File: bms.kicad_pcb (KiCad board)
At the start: 4 copper layers, 100 x 67 mm, 179 parts, among them J1 CELL_TAPS, J2 I2C_IN, J3 THERM_1, J4 THERM_2, J5 SWD, Q1 AO3400A, Q10 AO3400A, Q11 AO3400A, Q12 AO3400A, Q13 AO3400A, Q14 AO3400A, Q15 AO3400A, Q16 AO3400A, Q17 AO3400A, Q18 AO3400A, Q19 AO3400A, Q2 AO3400A, Q20 AO3400A, Q3 AO3400A, Q4 AO3400A, Q5 AO3400A, Q6 AO3400A, Q7 AO3400A, Q8 AO3400A, Q9 AO3400A, SW1 SW_Push, U1 LMR516xx, U2 STM32F103C8Tx, U3 ADuM1252, U4 MAX14920, U5 MAX11163, U6 MAX6126, Y1 8M

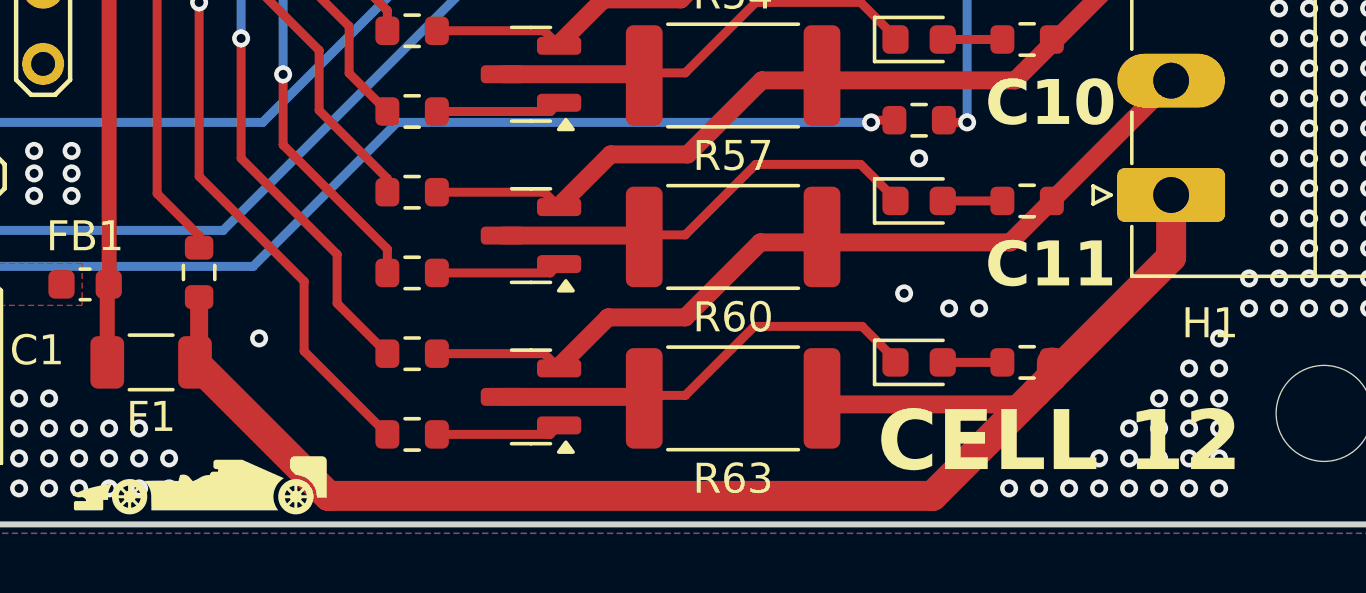
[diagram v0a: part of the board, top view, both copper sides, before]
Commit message: pcb: Reduce TAP12 trace width from 1 mm to 0.6 mm
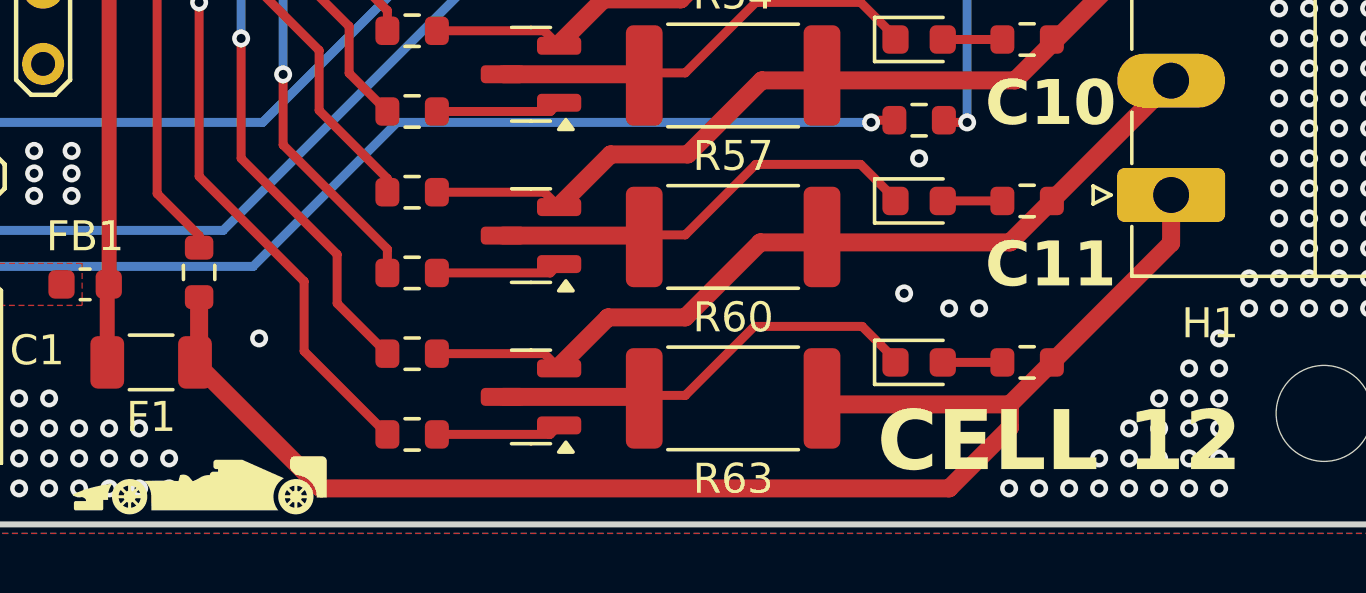
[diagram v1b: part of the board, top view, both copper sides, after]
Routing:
- net TAP12: track 49.8 -> 48.3 mm
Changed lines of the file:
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@@
 	(segment
 		(start 136.4 110.22)
-		(end 136.4 112.3)
-		(width 1)
+		(end 136.4 111.825)
+		(width 0.6)
 		(layer "F.Cu")
 		(net 70)
 	)
 	(segment
-		(start 128.45 120.25)
-		(end 131.9 116.8)
-		(width 1)
+		(start 131.025 117.2)
+		(end 132.425 115.8)
+		(width 0.6)
 		(layer "F.Cu")
 		(net 70)
@@
 	)
 	(segment
-		(start 136.4 112.3)
-		(end 132.425 116.275)
-		(width 1)
-		(layer "F.Cu")
-		(net 70)
-	)
-	(segment
-		(start 103.8625 115.8)
-		(end 108.3125 120.25)
-		(width 1)
-		(layer "F.Cu")
-		(net 70)
-	)
-	(segment
 		(start 104 115.6625)
 		(end 103.8625 115.8)
@@
 	)
 	(segment
-		(start 132.425 115.8)
-		(end 132.425 116.275)
-		(width 1)
+		(start 129 120)
+		(end 108.0625 120)
+		(width 0.6)
+		(layer "F.Cu")
+		(net 70)
+	)
+	(segment
+		(start 136.4 111.825)
+		(end 132.425 115.8)
+		(width 0.6)
+		(layer "F.Cu")
+		(net 70)
+	)
+	(segment
+		(start 131.025 117.975)
+		(end 131.025 117.2)
+		(width 0.6)
+		(layer "F.Cu")
+		(net 70)
+	)
+	(segment
+		(start 108.0625 120)
+		(end 103.8625 115.8)
+		(width 0.6)
 		(layer "F.Cu")
 		(net 70)
@@
 	(segment
 		(start 124.9625 117.2)
-		(end 131.5 117.2)
+		(end 131.025 117.2)
 		(width 0.6)
 		(layer "F.Cu")
@@
 	)
 	(segment
-		(start 108.3125 120.25)
-		(end 128.45 120.25)
-		(width 1)
-		(layer "F.Cu")
-		(net 70)
-	)
-	(segment
-		(start 132.425 116.275)
-		(end 131.9 116.8)
-		(width 1)
+		(start 129 120)
+		(end 131.025 117.975)
+		(width 0.6)
 		(layer "F.Cu")
 		(net 70)
@@
 		(width 0.6)
 		(layer "F.Cu")
-		(net 70)
-	)
-	(segment
-		(start 131.5 117.2)
-		(end 131.9 116.8)
-		(width 0.6)
-		(layer "F.Cu")

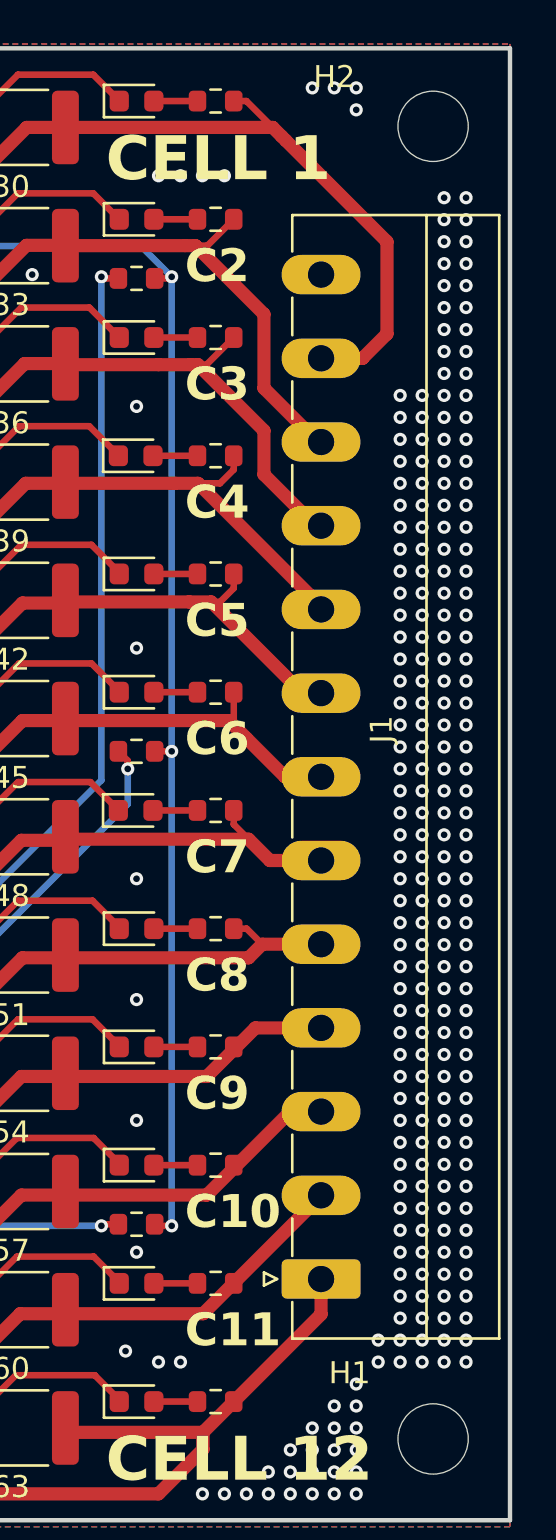
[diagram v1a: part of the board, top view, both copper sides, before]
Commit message: pcb: Move cell tap connector towards board edge by 0.3 mm
Closes GH-1
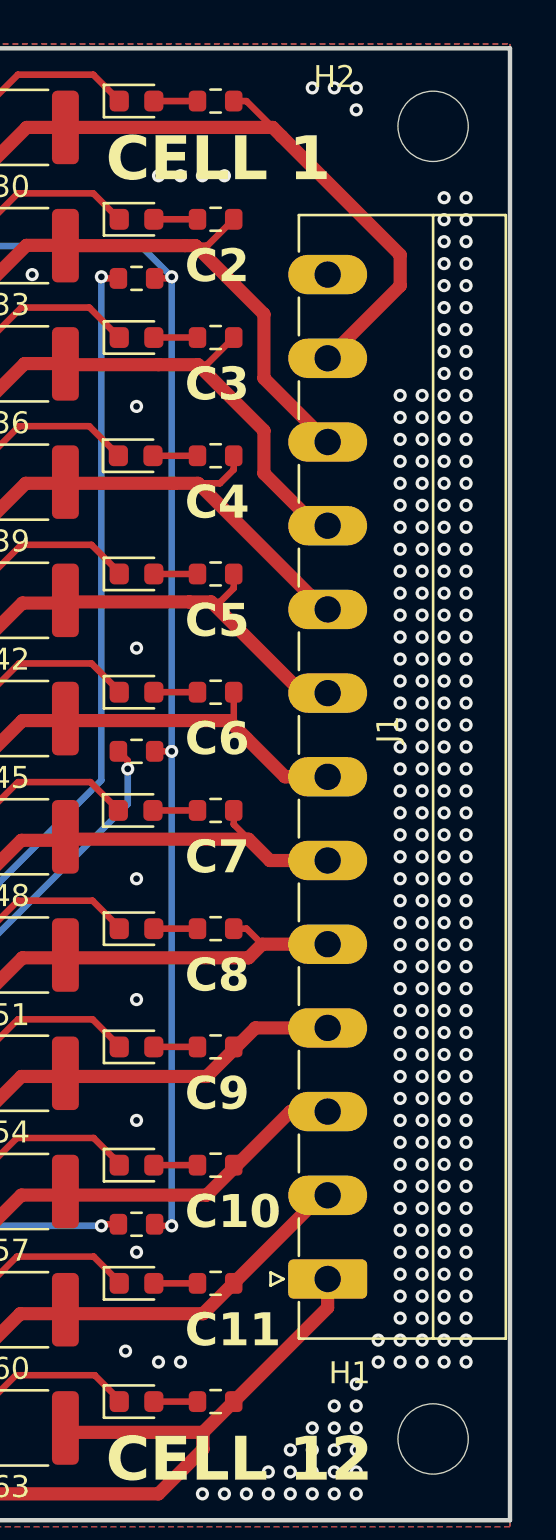
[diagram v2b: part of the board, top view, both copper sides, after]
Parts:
- moved J1 0.30 mm to (136.7, 110.2)
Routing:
- net TAP1: track 42.3 -> 41.4 mm
- net TAP11: track 28.8 -> 29.6 mm
- net TAP4: track 32.5 -> 33.1 mm

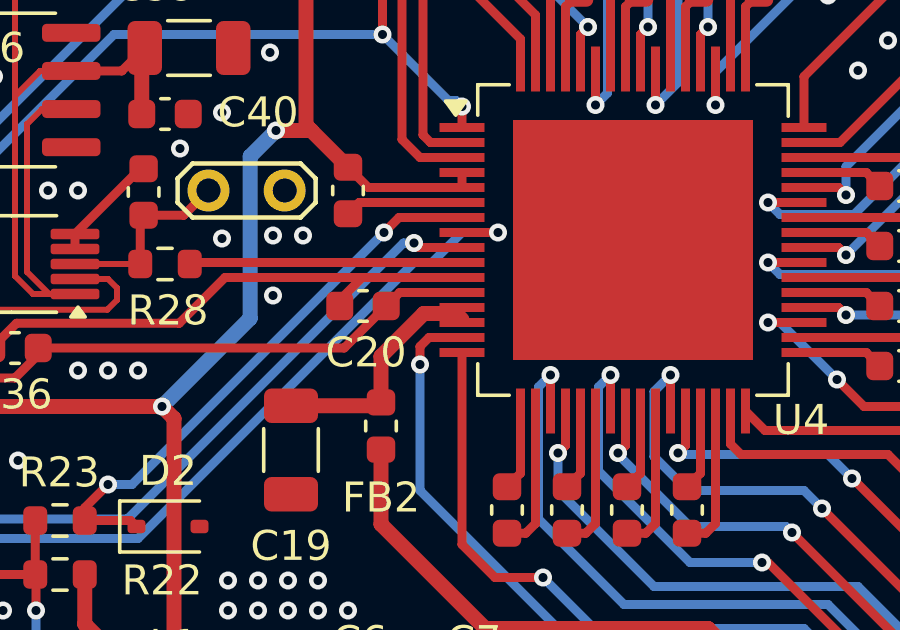
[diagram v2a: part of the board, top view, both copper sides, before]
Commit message: pcb: Use a filled zone for AFE_VIN
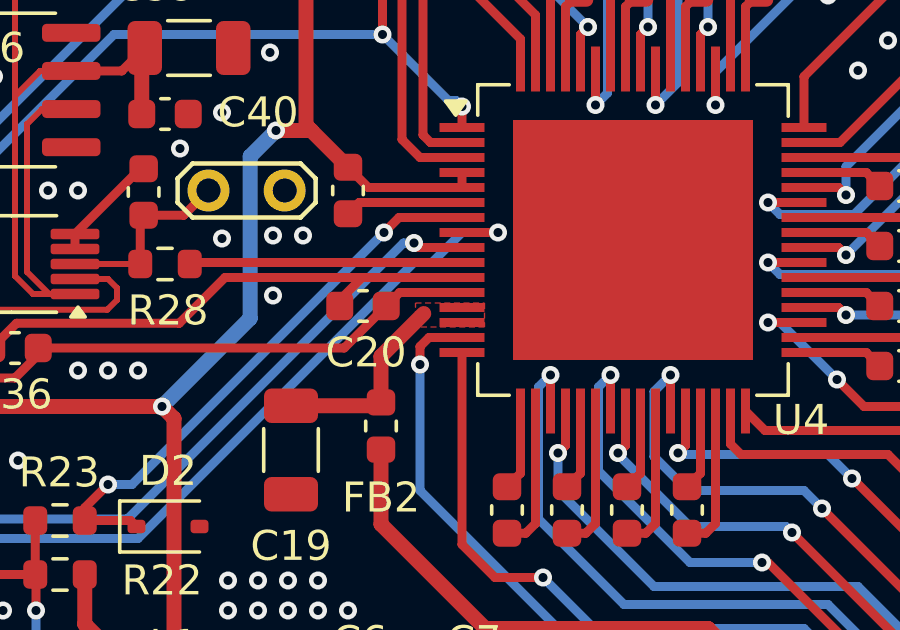
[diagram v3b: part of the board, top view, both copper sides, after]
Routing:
- net /AFE_VIN: track 7.96 -> 6.60 mm
- added copper zone on F.Cu, net /AFE_VIN
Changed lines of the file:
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@@
 	)
 	(segment
-		(start 90.6 90.1)
-		(end 90.8 90.3)
-		(width 0.5)
-		(layer "F.Cu")
-		(net 12)
-	)
-	(segment
 		(start 87.9875 93.174999)
 		(end 88.1 93.062499)
@@
 	)
 	(segment
-		(start 89.525736 90.1)
-		(end 90.6 90.1)
-		(width 0.5)
-		(layer "F.Cu")
-		(net 12)
-	)
-	(segment
 		(start 88.1 91.525736)
 		(end 89.525736 90.1)
@@
 			)
 		)
+	)
+	(zone
+		(net 12)
+		(net_name "/AFE_VIN")
+		(layer "F.Cu")
+		(hatch edge 0.5)
+		(priority 1)
+		(connect_pads yes
+			(clearance 0.15)
+		)
+		(min_thickness 0.25)
+		(filled_areas_thickness no)
+		(fill yes
+			(thermal_gap 0.5)
+			(thermal_bridge_width 0.5)
+		)
+		(polygon
+			(pts
+				(xy 89.25 89.75) (xy 91.55 89.75) (xy 91.55 90.55) (xy 89.25 90.55)
+			)
+		)

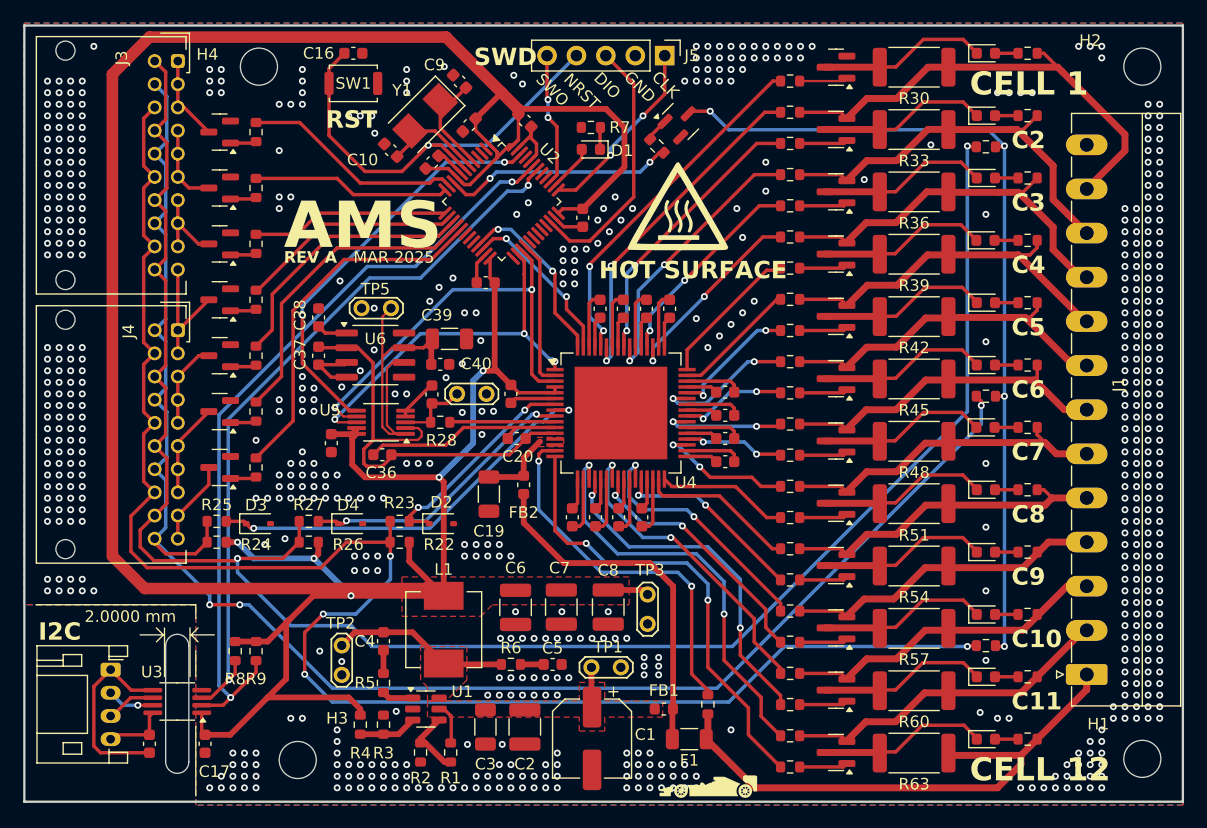
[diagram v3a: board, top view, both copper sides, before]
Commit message: pcb: Cleanup GND vias
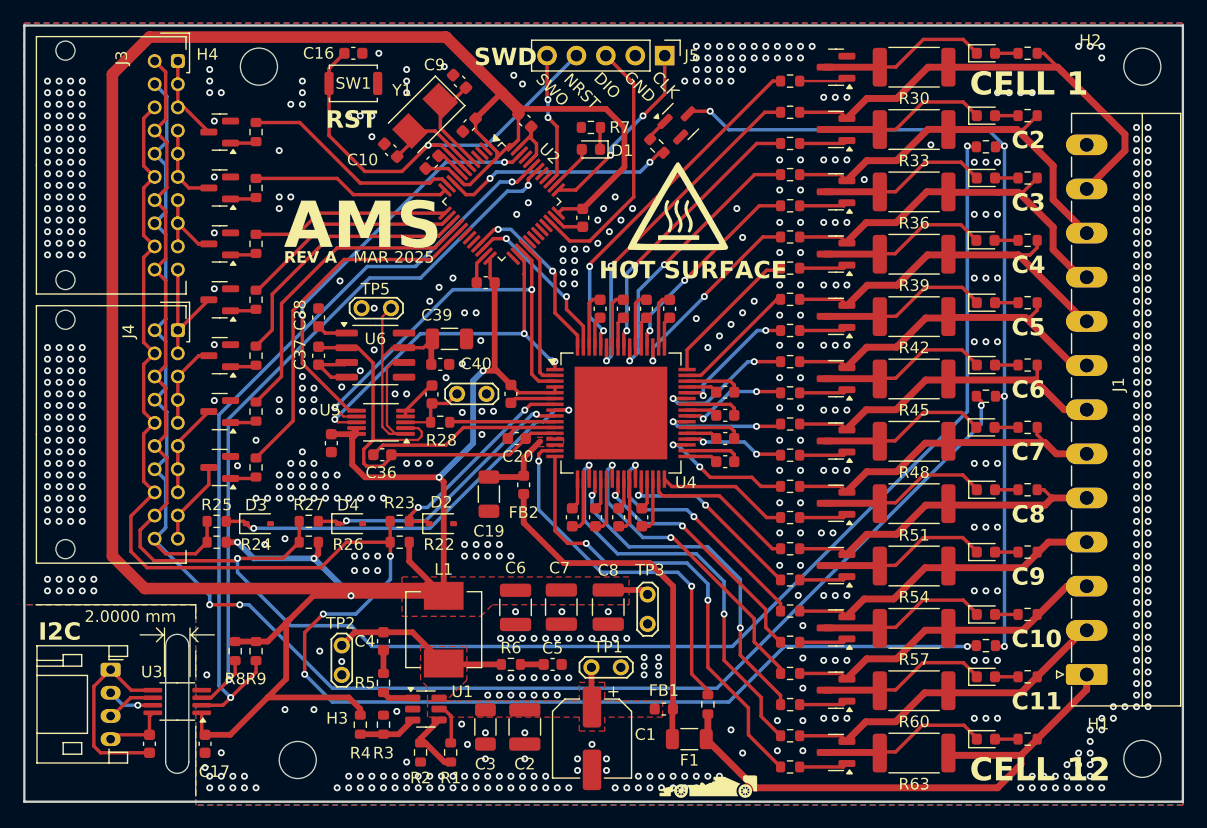
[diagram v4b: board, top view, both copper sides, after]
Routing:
- net GND: vias 673 -> 658
